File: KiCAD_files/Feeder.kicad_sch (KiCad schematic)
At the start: 61 parts, among them J505 Conn_01x03, Q501 60V N channel, Q502 TK13P25D,RQ, Q503 Q_Dual_NMOS_G1S2G2D2S1D1, Q504 Q_Dual_NMOS_G1S2G2D2S1D1, T501 PA2467NL, U501 NCP12700, U502 HMHA2801A, U503 TL431MFDT,215

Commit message: Feature Freeze PCB ordered
Former-commit-id: 656e77d39b103ec58b17965582500bfb0a5b80a0
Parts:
- removed Q503, Q504: Q_Dual_NMOS_G1S2G2D2S1D1, symbol Device:Q_Dual_NMOS_G1S2G2D2S1D1
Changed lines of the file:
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@@
-    (stroke (width 0) (type default) (color 0 0 0 0))
-  )
-  (wire (pts (xy 71.755 223.52) (xy 71.755 224.79))
     (stroke (width 0) (type default) (color 0 0 0 0))
   )
@@
     (stroke (width 0) (type default) (color 0 0 0 0))
   )
-  (wire (pts (xy 121.285 234.95) (xy 121.285 238.76))
-    (stroke (width 0) (type default) (color 0 0 0 0))
-  )
   (wire (pts (xy 113.03 88.265) (xy 113.03 75.565))
     (stroke (width 0) (type default) (color 0 0 0 0))
@@
   )
   (wire (pts (xy 237.49 103.505) (xy 237.49 104.775))
-    (stroke (width 0.45) (type default) (color 0 0 0 0))
-  )
-  (wire (pts (xy 121.285 238.76) (xy 121.285 241.3))
     (stroke (width 0.45) (type default) (color 0 0 0 0))
   )
@@
     (stroke (width 0) (type default) (color 0 0 0 0))
   )
-  (wire (pts (xy 71.755 206.375) (xy 80.01 206.375))
-    (stroke (width 0) (type default) (color 0 0 0 0))
-  )
   (wire (pts (xy 196.85 104.775) (xy 205.105 104.775))
     (stroke (width 0) (type default) (color 0 0 0 0))
@@
     (stroke (width 0) (type default) (color 0 0 0 0))
   )
-  (wire (pts (xy 71.755 213.36) (xy 71.755 206.375))
-    (stroke (width 0) (type default) (color 0 0 0 0))
-  )
   (wire (pts (xy 180.975 94.615) (xy 180.975 90.805))
     (stroke (width 0) (type default) (color 0 0 0 0))
@@
   (wire (pts (xy 284.48 177.165) (xy 281.94 177.165))
     (stroke (width 0) (type default) (color 0 0 0 0))
-  )
-  (wire (pts (xy 71.755 238.76) (xy 71.755 241.3))
-    (stroke (width 0.45) (type default) (color 0 0 0 0))
   )
   (wire (pts (xy 162.56 125.73) (xy 162.56 139.7))
@@
     (stroke (width 0) (type default) (color 0 0 0 0))
   )
-  (wire (pts (xy 121.285 241.3) (xy 121.285 242.57))
-    (stroke (width 0) (type default) (color 0 0 0 0))
-  )
   (wire (pts (xy 180.975 104.775) (xy 196.85 104.775))
     (stroke (width 0) (type default) (color 0 0 0 0))
@@
     (stroke (width 0) (type default) (color 0 0 0 0))
   )
-  (wire (pts (xy 121.285 213.36) (xy 121.285 206.375))
-    (stroke (width 0) (type default) (color 0 0 0 0))
-  )
   (wire (pts (xy 222.885 24.13) (xy 222.885 26.035))
     (stroke (width 0) (type default) (color 0 0 0 0))
@@
   )
   (wire (pts (xy 90.17 139.7) (xy 90.17 146.05))
-    (stroke (width 0) (type default) (color 0 0 0 0))
-  )
-  (wire (pts (xy 121.285 206.375) (xy 129.54 206.375))
     (stroke (width 0) (type default) (color 0 0 0 0))
   )
@@
     (stroke (width 0.15) (type default) (color 0 0 0 0))
   )
-  (wire (pts (xy 71.755 234.95) (xy 71.755 238.76))
-    (stroke (width 0) (type default) (color 0 0 0 0))
-  )
   (wire (pts (xy 60.96 47.625) (xy 60.96 60.325))
     (stroke (width 0) (type default) (color 0 0 0 0))
@@
   )
   (wire (pts (xy 170.815 83.185) (xy 169.545 83.185))
-    (stroke (width 0) (type default) (color 0 0 0 0))
-  )
-  (wire (pts (xy 121.285 223.52) (xy 121.285 224.79))
     (stroke (width 0) (type default) (color 0 0 0 0))
   )
@@
     (effects (font (size 1.27 1.27)) (justify left bottom))
   )
-  (label "GND_Supply" (at 80.01 206.375 0)
-    (effects (font (size 1.27 1.27)) (justify left bottom))
-  )
   (label "+6VJP" (at 316.23 85.09 180)
     (effects (font (size 1.27 1.27)) (justify right bottom))
-  )
-  (label "GND_Supply" (at 129.54 206.375 0)
-    (effects (font (size 1.27 1.27)) (justify left bottom))
   )
   (label "VAUX" (at 187.96 124.46 0)
@@
     )
     (pin "1")
-  )
-  (symbol (lib_id "Device:Q_Dual_NMOS_G1S2G2D2S1D1") (at 118.745 229.87 0) (mirror x) (unit 1)
-    (in_bom yes) (on_board yes) (fields_autoplaced)
-    (property "Reference" "Q504" (id 0) (at 124.46 228.5999 0)
-      (effects (font (size 1.27 1.27)) (justify left))
-    )
-    (property "Value" "Q_Dual_NMOS_G1S2G2D2S1D1" (id 1) (at 124.46 231.1399 0)
-      (effects (font (size 1.27 1.27)) (justify left))
-    )
-    (property "Footprint" "" (id 2) (at 123.825 229.87 0)
-      (effects (font (size 1.27 1.27)) hide)
-    )
-    (property "Datasheet" "~" (id 3) (at 123.825 229.87 0)
-      (effects (font (size 1.27 1.27)) hide)
-    )
-    (pin "1")
-    (pin "5")
-    (pin "6")
   )
   (symbol (lib_id "Device:C") (at 229.87 38.735 90) (unit 1)
@@
     (pin "2")
   )
-  (symbol (lib_id "Device:Q_Dual_NMOS_G1S2G2D2S1D1") (at 69.215 229.87 0) (mirror x) (unit 1)
-    (in_bom yes) (on_board yes) (fields_autoplaced)
-    (property "Reference" "Q503" (id 0) (at 74.93 228.5999 0)
-      (effects (font (size 1.27 1.27)) (justify left))
-    )
-    (property "Value" "Q_Dual_NMOS_G1S2G2D2S1D1" (id 1) (at 74.93 231.1399 0)
-      (effects (font (size 1.27 1.27)) (justify left))
-    )
-    (property "Footprint" "" (id 2) (at 74.295 229.87 0)
-      (effects (font (size 1.27 1.27)) hide)
-    )
-    (property "Datasheet" "~" (id 3) (at 74.295 229.87 0)
-      (effects (font (size 1.27 1.27)) hide)
-    )
-    (pin "1")
-    (pin "5")
-    (pin "6")
-  )
   (symbol (lib_id "Device:Q_NMOS_GSD") (at 179.705 135.89 0) (mirror y) (unit 1)
     (in_bom yes) (on_board yes)
@@
     (pin "9")
   )
-  (symbol (lib_id "power:GND") (at 71.755 241.3 0) (unit 1)
-    (in_bom yes) (on_board yes)
-    (property "Reference" "#PWR0161" (id 0) (at 71.755 247.65 0)
-      (effects (font (size 1.27 1.27)) hide)
-    )
-    (property "Value" "GND" (id 1) (at 71.755 246.38 0))
-    (property "Footprint" "" (id 2) (at 71.755 241.3 0)
-      (effects (font (size 1.27 1.27)) hide)
-    )
-    (property "Datasheet" "" (id 3) (at 71.755 241.3 0)
-      (effects (font (size 1.27 1.27)) hide)
-    )
-    (pin "1")
-  )
   (symbol (lib_id "Device:L") (at 41.91 47.625 90) (unit 1)
     (in_bom yes) (on_board yes) (fields_autoplaced)
@@
     (pin "2")
   )
-  (symbol (lib_id "Symbols:NGND") (at 121.285 242.57 0) (unit 1)
-    (in_bom yes) (on_board yes)
-    (property "Reference" "#PWR0162" (id 0) (at 121.285 248.92 0)
-      (effects (font (size 1.27 1.27)) hide)
-    )
-    (property "Value" "NGND" (id 1) (at 117.475 243.205 0))
-    (property "Footprint" "" (id 2) (at 121.285 242.57 0)
-      (effects (font (size 1.27 1.27)) hide)
-    )
-    (property "Datasheet" "" (id 3) (at 121.285 242.57 0)
-      (effects (font (size 1.27 1.27)) hide)
-    )
-    (pin "1")
-  )
   (symbol (lib_id "Device:C") (at 35.56 64.135 0) (unit 1)
     (in_bom yes) (on_board yes)
@@
     (pin "2")
   )
-  (symbol (lib_id "Device:Q_Dual_NMOS_G1S2G2D2S1D1") (at 69.215 218.44 0) (unit 2)
-    (in_bom yes) (on_board yes) (fields_autoplaced)
-    (property "Reference" "Q503" (id 0) (at 75.565 217.1699 0)
-      (effects (font (size 1.27 1.27)) (justify left))
-    )
-    (property "Value" "Q_Dual_NMOS_G1S2G2D2S1D1" (id 1) (at 75.565 219.7099 0)
-      (effects (font (size 1.27 1.27)) (justify left))
-    )
-    (property "Footprint" "" (id 2) (at 74.295 218.44 0)
-      (effects (font (size 1.27 1.27)) hide)
-    )
-    (property "Datasheet" "~" (id 3) (at 74.295 218.44 0)
-      (effects (font (size 1.27 1.27)) hide)
-    )
-    (pin "2")
-    (pin "3")
-    (pin "4")
-  )
   (symbol (lib_id "Symbols:V1.1.2") (at 105.41 88.9 0) (unit 1)
     (in_bom yes) (on_board yes)
@@
     (pin "2")
   )
-  (symbol (lib_id "Device:Q_Dual_NMOS_G1S2G2D2S1D1") (at 118.745 218.44 0) (unit 2)
-    (in_bom yes) (on_board yes) (fields_autoplaced)
-    (property "Reference" "Q504" (id 0) (at 125.095 217.1699 0)
-      (effects (font (size 1.27 1.27)) (justify left))
-    )
-    (property "Value" "Q_Dual_NMOS_G1S2G2D2S1D1" (id 1) (at 125.095 219.7099 0)
-      (effects (font (size 1.27 1.27)) (justify left))
-    )
-    (property "Footprint" "" (id 2) (at 123.825 218.44 0)
-      (effects (font (size 1.27 1.27)) hide)
-    )
-    (property "Datasheet" "~" (id 3) (at 123.825 218.44 0)
-      (effects (font (size 1.27 1.27)) hide)
-    )
-    (pin "2")
-    (pin "3")
-    (pin "4")
-  )
   (symbol (lib_id "Symbols:V1.1.2") (at 292.1 184.15 0) (unit 1)

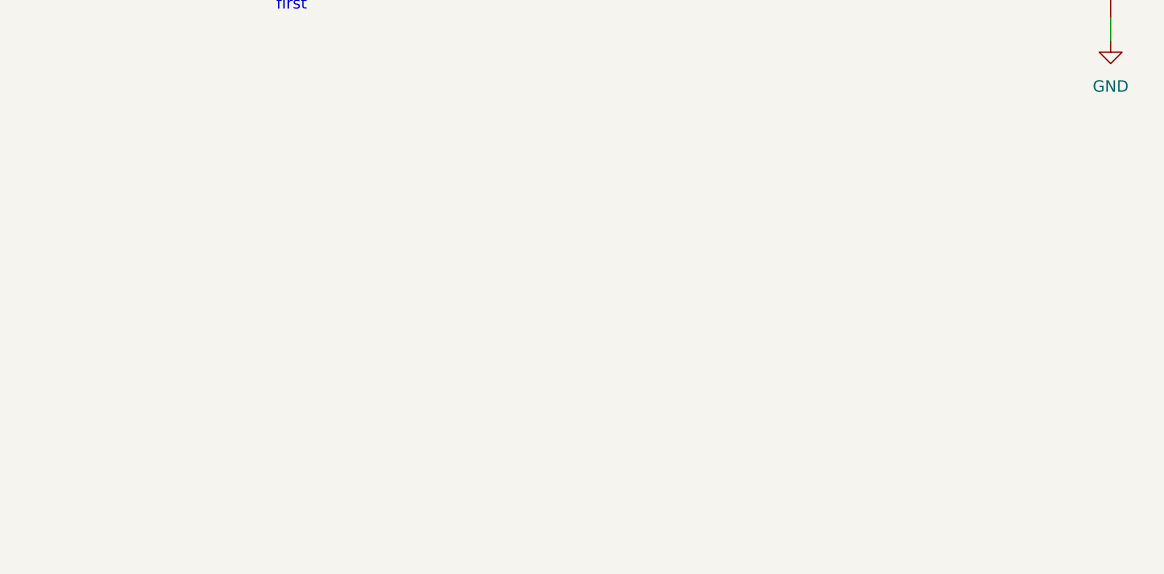
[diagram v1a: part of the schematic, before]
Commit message: WIP: added features for the RJ45 communication link. Added fast RS485 Added HRTIM Sync Added current share analog bus Added external VREF Added dedicated supply power supply pins for the data manager
Former-commit-id: 7d7dbd6688aaf47caa2ea5f91bf9cef552f6a24c
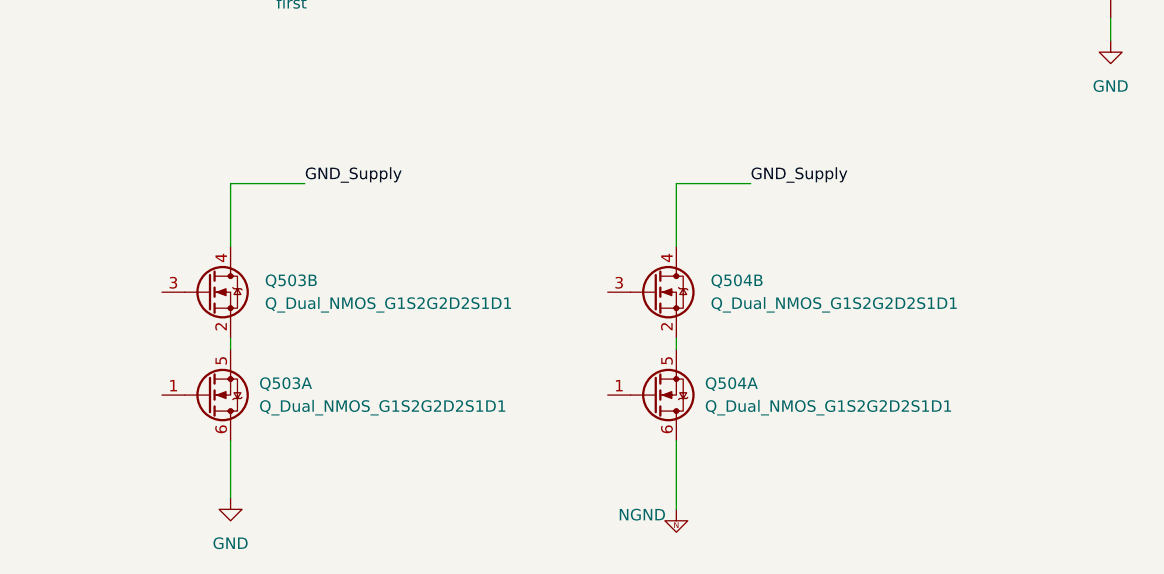
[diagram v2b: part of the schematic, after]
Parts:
- added Q503, Q504: Q_Dual_NMOS_G1S2G2D2S1D1, symbol Device:Q_Dual_NMOS_G1S2G2D2S1D1
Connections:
- net GND: now also Q503.6 (D)
- new net: Q504.2 (S), Q504.5 (S)
- new net: Q503.2 (S), Q503.5 (S)
- new net GND_Supply: Q503.4 (D), Q504.4 (D)
- new net NGND: Q504.6 (D)
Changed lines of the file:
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@@
+    (stroke (width 0) (type default) (color 0 0 0 0))
+  )
+  (wire (pts (xy 71.755 223.52) (xy 71.755 224.79))
     (stroke (width 0) (type default) (color 0 0 0 0))
   )
@@
     (stroke (width 0) (type default) (color 0 0 0 0))
   )
+  (wire (pts (xy 121.285 234.95) (xy 121.285 238.76))
+    (stroke (width 0) (type default) (color 0 0 0 0))
+  )
   (wire (pts (xy 113.03 88.265) (xy 113.03 75.565))
     (stroke (width 0) (type default) (color 0 0 0 0))
@@
   )
   (wire (pts (xy 237.49 103.505) (xy 237.49 104.775))
+    (stroke (width 0.45) (type default) (color 0 0 0 0))
+  )
+  (wire (pts (xy 121.285 238.76) (xy 121.285 241.3))
     (stroke (width 0.45) (type default) (color 0 0 0 0))
   )
@@
     (stroke (width 0) (type default) (color 0 0 0 0))
   )
+  (wire (pts (xy 71.755 206.375) (xy 80.01 206.375))
+    (stroke (width 0) (type default) (color 0 0 0 0))
+  )
   (wire (pts (xy 196.85 104.775) (xy 205.105 104.775))
     (stroke (width 0) (type default) (color 0 0 0 0))
@@
     (stroke (width 0) (type default) (color 0 0 0 0))
   )
+  (wire (pts (xy 71.755 213.36) (xy 71.755 206.375))
+    (stroke (width 0) (type default) (color 0 0 0 0))
+  )
   (wire (pts (xy 180.975 94.615) (xy 180.975 90.805))
     (stroke (width 0) (type default) (color 0 0 0 0))
@@
   (wire (pts (xy 284.48 177.165) (xy 281.94 177.165))
     (stroke (width 0) (type default) (color 0 0 0 0))
+  )
+  (wire (pts (xy 71.755 238.76) (xy 71.755 241.3))
+    (stroke (width 0.45) (type default) (color 0 0 0 0))
   )
   (wire (pts (xy 162.56 125.73) (xy 162.56 139.7))
@@
     (stroke (width 0) (type default) (color 0 0 0 0))
   )
+  (wire (pts (xy 121.285 241.3) (xy 121.285 242.57))
+    (stroke (width 0) (type default) (color 0 0 0 0))
+  )
   (wire (pts (xy 180.975 104.775) (xy 196.85 104.775))
     (stroke (width 0) (type default) (color 0 0 0 0))
@@
     (stroke (width 0) (type default) (color 0 0 0 0))
   )
+  (wire (pts (xy 121.285 213.36) (xy 121.285 206.375))
+    (stroke (width 0) (type default) (color 0 0 0 0))
+  )
   (wire (pts (xy 222.885 24.13) (xy 222.885 26.035))
     (stroke (width 0) (type default) (color 0 0 0 0))
@@
   )
   (wire (pts (xy 90.17 139.7) (xy 90.17 146.05))
+    (stroke (width 0) (type default) (color 0 0 0 0))
+  )
+  (wire (pts (xy 121.285 206.375) (xy 129.54 206.375))
     (stroke (width 0) (type default) (color 0 0 0 0))
   )
@@
     (stroke (width 0.15) (type default) (color 0 0 0 0))
   )
+  (wire (pts (xy 71.755 234.95) (xy 71.755 238.76))
+    (stroke (width 0) (type default) (color 0 0 0 0))
+  )
   (wire (pts (xy 60.96 47.625) (xy 60.96 60.325))
     (stroke (width 0) (type default) (color 0 0 0 0))
@@
   )
   (wire (pts (xy 170.815 83.185) (xy 169.545 83.185))
+    (stroke (width 0) (type default) (color 0 0 0 0))
+  )
+  (wire (pts (xy 121.285 223.52) (xy 121.285 224.79))
     (stroke (width 0) (type default) (color 0 0 0 0))
   )
@@
     (effects (font (size 1.27 1.27)) (justify left bottom))
   )
+  (label "GND_Supply" (at 80.01 206.375 0)
+    (effects (font (size 1.27 1.27)) (justify left bottom))
+  )
   (label "+6VJP" (at 316.23 85.09 180)
     (effects (font (size 1.27 1.27)) (justify right bottom))
+  )
+  (label "GND_Supply" (at 129.54 206.375 0)
+    (effects (font (size 1.27 1.27)) (justify left bottom))
   )
   (label "VAUX" (at 187.96 124.46 0)
@@
     )
     (pin "1")
+  )
+  (symbol (lib_id "Device:Q_Dual_NMOS_G1S2G2D2S1D1") (at 118.745 229.87 0) (mirror x) (unit 1)
+    (in_bom yes) (on_board yes) (fields_autoplaced)
+    (property "Reference" "Q504" (id 0) (at 124.46 228.5999 0)
+      (effects (font (size 1.27 1.27)) (justify left))
+    )
+    (property "Value" "Q_Dual_NMOS_G1S2G2D2S1D1" (id 1) (at 124.46 231.1399 0)
+      (effects (font (size 1.27 1.27)) (justify left))
+    )
+    (property "Footprint" "" (id 2) (at 123.825 229.87 0)
+      (effects (font (size 1.27 1.27)) hide)
+    )
+    (property "Datasheet" "~" (id 3) (at 123.825 229.87 0)
+      (effects (font (size 1.27 1.27)) hide)
+    )
+    (pin "1")
+    (pin "5")
+    (pin "6")
   )
   (symbol (lib_id "Device:C") (at 229.87 38.735 90) (unit 1)
@@
     (pin "2")
   )
+  (symbol (lib_id "Device:Q_Dual_NMOS_G1S2G2D2S1D1") (at 69.215 229.87 0) (mirror x) (unit 1)
+    (in_bom yes) (on_board yes) (fields_autoplaced)
+    (property "Reference" "Q503" (id 0) (at 74.93 228.5999 0)
+      (effects (font (size 1.27 1.27)) (justify left))
+    )
+    (property "Value" "Q_Dual_NMOS_G1S2G2D2S1D1" (id 1) (at 74.93 231.1399 0)
+      (effects (font (size 1.27 1.27)) (justify left))
+    )
+    (property "Footprint" "" (id 2) (at 74.295 229.87 0)
+      (effects (font (size 1.27 1.27)) hide)
+    )
+    (property "Datasheet" "~" (id 3) (at 74.295 229.87 0)
+      (effects (font (size 1.27 1.27)) hide)
+    )
+    (pin "1")
+    (pin "5")
+    (pin "6")
+  )
   (symbol (lib_id "Device:Q_NMOS_GSD") (at 179.705 135.89 0) (mirror y) (unit 1)
     (in_bom yes) (on_board yes)
@@
     (pin "9")
   )
+  (symbol (lib_id "power:GND") (at 71.755 241.3 0) (unit 1)
+    (in_bom yes) (on_board yes)
+    (property "Reference" "#PWR0161" (id 0) (at 71.755 247.65 0)
+      (effects (font (size 1.27 1.27)) hide)
+    )
+    (property "Value" "GND" (id 1) (at 71.755 246.38 0))
+    (property "Footprint" "" (id 2) (at 71.755 241.3 0)
+      (effects (font (size 1.27 1.27)) hide)
+    )
+    (property "Datasheet" "" (id 3) (at 71.755 241.3 0)
+      (effects (font (size 1.27 1.27)) hide)
+    )
+    (pin "1")
+  )
   (symbol (lib_id "Device:L") (at 41.91 47.625 90) (unit 1)
     (in_bom yes) (on_board yes) (fields_autoplaced)
@@
     (pin "2")
   )
+  (symbol (lib_id "Symbols:NGND") (at 121.285 242.57 0) (unit 1)
+    (in_bom yes) (on_board yes)
+    (property "Reference" "#PWR0162" (id 0) (at 121.285 248.92 0)
+      (effects (font (size 1.27 1.27)) hide)
+    )
+    (property "Value" "NGND" (id 1) (at 117.475 243.205 0))
+    (property "Footprint" "" (id 2) (at 121.285 242.57 0)
+      (effects (font (size 1.27 1.27)) hide)
+    )
+    (property "Datasheet" "" (id 3) (at 121.285 242.57 0)
+      (effects (font (size 1.27 1.27)) hide)
+    )
+    (pin "1")
+  )
   (symbol (lib_id "Device:C") (at 35.56 64.135 0) (unit 1)
     (in_bom yes) (on_board yes)
@@
     (pin "2")
   )
+  (symbol (lib_id "Device:Q_Dual_NMOS_G1S2G2D2S1D1") (at 69.215 218.44 0) (unit 2)
+    (in_bom yes) (on_board yes) (fields_autoplaced)
+    (property "Reference" "Q503" (id 0) (at 75.565 217.1699 0)
+      (effects (font (size 1.27 1.27)) (justify left))
+    )
+    (property "Value" "Q_Dual_NMOS_G1S2G2D2S1D1" (id 1) (at 75.565 219.7099 0)
+      (effects (font (size 1.27 1.27)) (justify left))
+    )
+    (property "Footprint" "" (id 2) (at 74.295 218.44 0)
+      (effects (font (size 1.27 1.27)) hide)
+    )
+    (property "Datasheet" "~" (id 3) (at 74.295 218.44 0)
+      (effects (font (size 1.27 1.27)) hide)
+    )
+    (pin "2")
+    (pin "3")
+    (pin "4")
+  )
   (symbol (lib_id "Symbols:V1.1.2") (at 105.41 88.9 0) (unit 1)
     (in_bom yes) (on_board yes)
@@
     (pin "2")
   )
+  (symbol (lib_id "Device:Q_Dual_NMOS_G1S2G2D2S1D1") (at 118.745 218.44 0) (unit 2)
+    (in_bom yes) (on_board yes) (fields_autoplaced)
+    (property "Reference" "Q504" (id 0) (at 125.095 217.1699 0)
+      (effects (font (size 1.27 1.27)) (justify left))
+    )
+    (property "Value" "Q_Dual_NMOS_G1S2G2D2S1D1" (id 1) (at 125.095 219.7099 0)
+      (effects (font (size 1.27 1.27)) (justify left))
+    )
+    (property "Footprint" "" (id 2) (at 123.825 218.44 0)
+      (effects (font (size 1.27 1.27)) hide)
+    )
+    (property "Datasheet" "~" (id 3) (at 123.825 218.44 0)
+      (effects (font (size 1.27 1.27)) hide)
+    )
+    (pin "2")
+    (pin "3")
+    (pin "4")
+  )
   (symbol (lib_id "Symbols:V1.1.2") (at 292.1 184.15 0) (unit 1)
